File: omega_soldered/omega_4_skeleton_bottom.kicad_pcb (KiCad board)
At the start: 2 copper layers, 204.8 x 88 mm, 0 parts

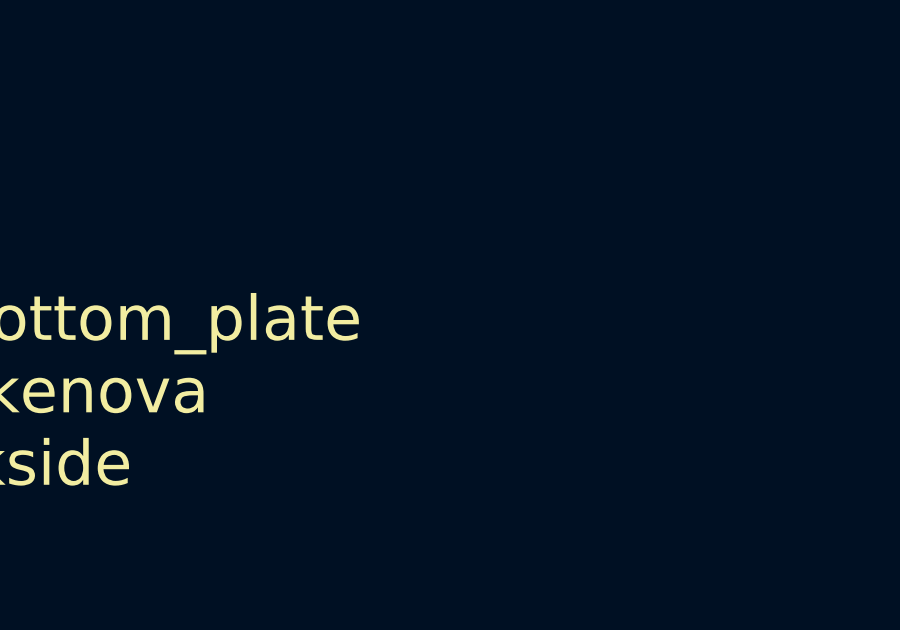
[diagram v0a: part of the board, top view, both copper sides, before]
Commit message: add jumper to skeleton case
jumper get the solder mask to show up
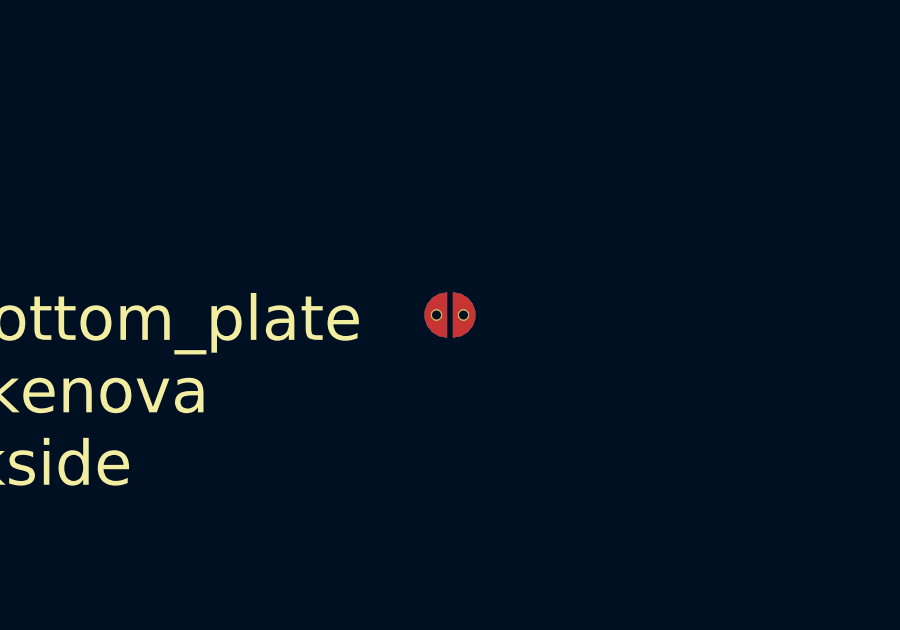
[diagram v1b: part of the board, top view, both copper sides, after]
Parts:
- added JP1: Jumper_NO_Small, Keebio-Parts:solder_jumper, F.Cu at (154.7, 112.9)
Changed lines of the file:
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@@
     (tracks 1)
     (zones 0)
-    (modules 0)
-    (nets 2)
+    (modules 1)
+    (nets 4)
   )
   (page A4)
@@
   (net 0 "")
   (net 1 GND)
+  (net 2 "Net-(JP1-Pad2)")
+  (net 3 "Net-(JP1-Pad1)")
   (net_class Default "This is the default net class."
     (clearance 0.2)
@@
     (uvia_dia 0.3)
     (uvia_drill 0.1)
+    (add_net "Net-(JP1-Pad1)")
+    (add_net "Net-(JP1-Pad2)")
+  )
+  (module Keebio-Parts:solder_jumper (layer F.Cu)
+    (at 154.725 112.875)
+    (solder_mask_margin 0.001)
+    (solder_paste_margin -0.02)
+    (clearance 0.001)
+    (fp_text reference JP1 (at -0.508 1.016) (layer Cmts.User) hide
+      (effects (font (size 0.3 0.3) (thickness 0.03)))
+    )
+    (fp_text value Jumper_NO_Small (at 0 -1.524) (layer F.SilkS) hide
+      (effects (font (size 0.4 0.4) (thickness 0.04)))
+    )
+    (fp_poly (pts (xy 0.1 0.75) (xy 0.3565 0.7048) (xy 0.5821 0.5745) (xy 0.7495 0.375)
+      (xy 0.8386 0.1302) (xy 0.8386 -0.1302) (xy 0.7495 -0.375) (xy 0.5821 -0.5745)
+      (xy 0.3565 -0.7048) (xy 0.1 -0.75) (xy 0.1 0.75)) (layer B.Cu) (width 0.01))
+    (fp_poly (pts (xy -0.1 -0.75) (xy -0.3565 -0.7048) (xy -0.5821 -0.5745) (xy -0.7495 -0.375)
+      (xy -0.8386 -0.1302) (xy -0.8386 0.1302) (xy -0.7495 0.375) (xy -0.5821 0.5745)
+      (xy -0.3565 0.7048) (xy -0.1 0.75) (xy -0.1 -0.75)) (layer B.Cu) (width 0.01))
+    (fp_poly (pts (xy 0.1 0.75) (xy 0.3565 0.7048) (xy 0.5821 0.5745) (xy 0.7495 0.375)
+      (xy 0.8386 0.1302) (xy 0.8386 -0.1302) (xy 0.7495 -0.375) (xy 0.5821 -0.5745)
+      (xy 0.3565 -0.7048) (xy 0.1 -0.75) (xy 0.1 0.75)) (layer F.Cu) (width 0.01))
+    (fp_poly (pts (xy -0.1 -0.75) (xy -0.3565 -0.7048) (xy -0.5821 -0.5745) (xy -0.7495 -0.375)
+      (xy -0.8386 -0.1302) (xy -0.8386 0.1302) (xy -0.7495 0.375) (xy -0.5821 0.5745)
+      (xy -0.3565 0.7048) (xy -0.1 0.75) (xy -0.1 -0.75)) (layer F.Cu) (width 0.01))
+    (pad 2 thru_hole circle (at 0.45 0) (size 0.4 0.4) (drill 0.3) (layers *.Cu *.Mask)
+      (net 2 "Net-(JP1-Pad2)"))
+    (pad 1 thru_hole circle (at -0.45 0) (size 0.4 0.4) (drill 0.3) (layers *.Cu *.Mask)
+      (net 3 "Net-(JP1-Pad1)"))
   )
   (gr_text "omega_4_bottom_plate\nby makenova\ndarkside" (at 139.725 115.425) (layer F.SilkS)

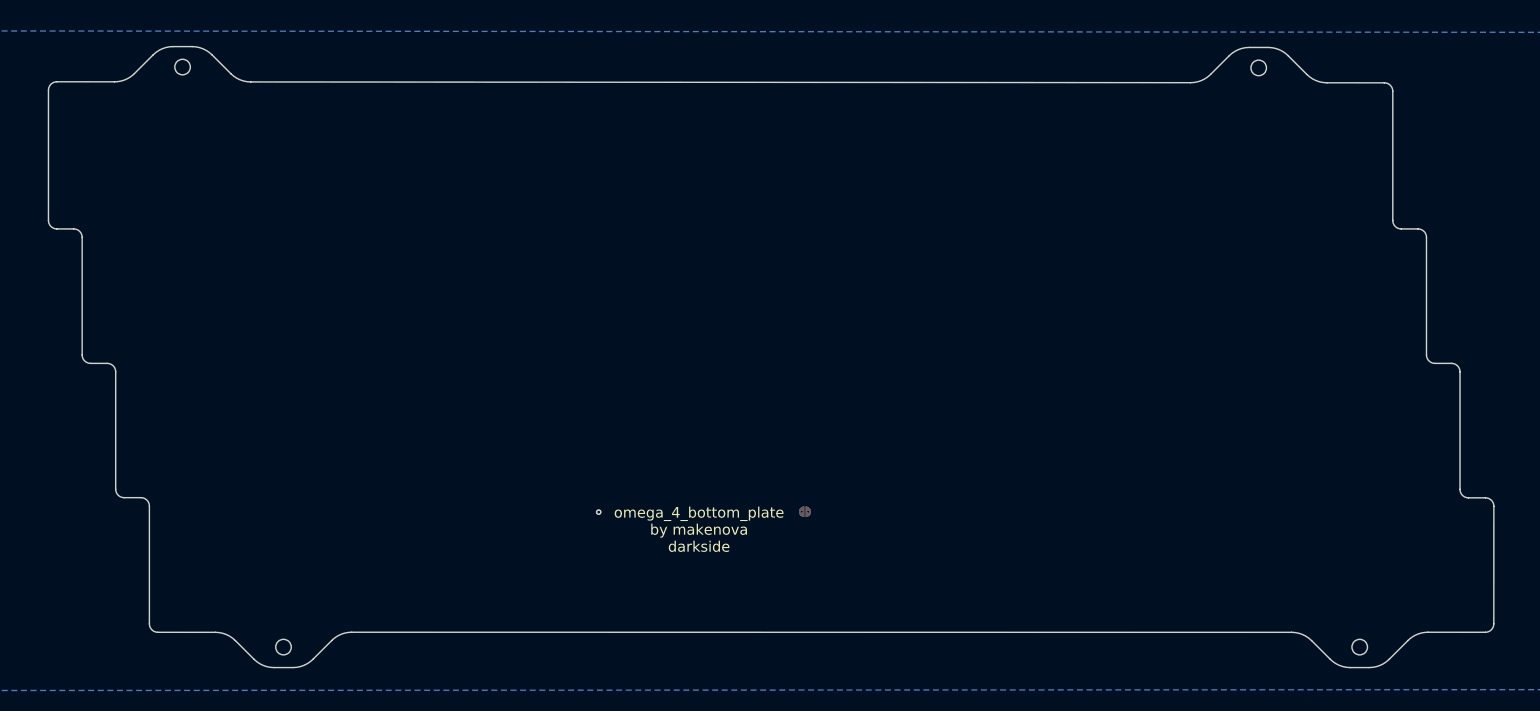
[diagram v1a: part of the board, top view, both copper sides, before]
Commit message: update skeleton case to allow 3mm between cuts and regen prod files
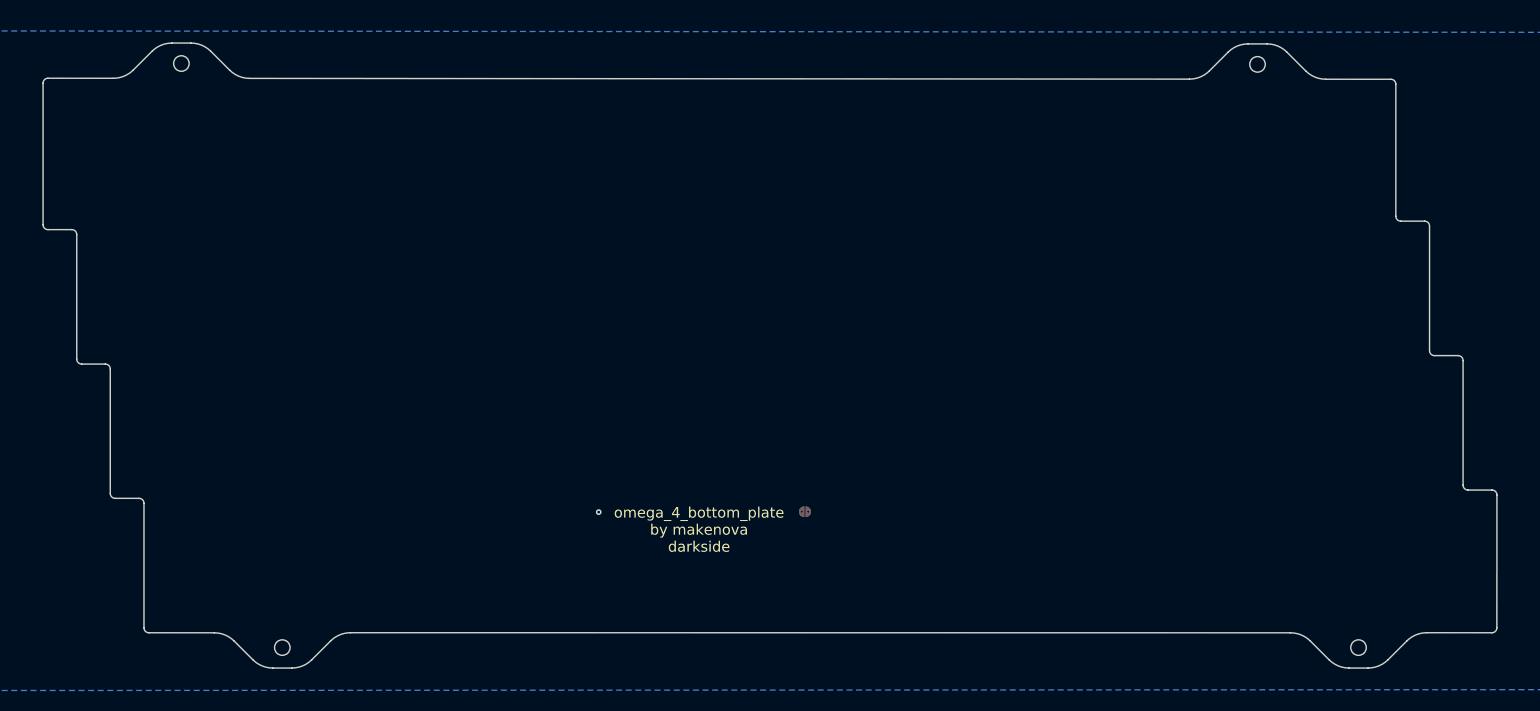
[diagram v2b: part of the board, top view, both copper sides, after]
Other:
- board size 204.8 x 88 mm -> 206 x 88.6 mm
